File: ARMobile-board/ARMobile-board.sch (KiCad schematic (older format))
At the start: 10 parts

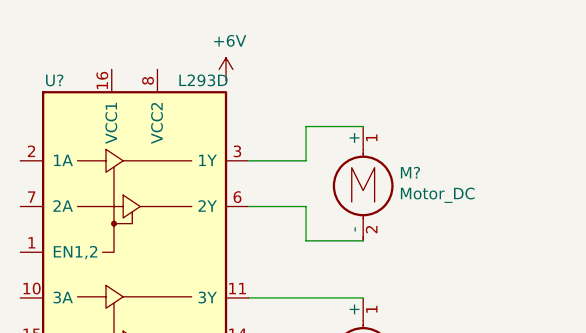
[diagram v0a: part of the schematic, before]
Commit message: Fixed schematic mistake (not connected pr)
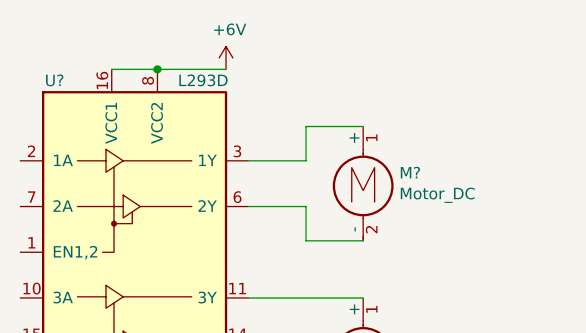
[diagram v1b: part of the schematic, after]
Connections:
- net +6V: now also U?.16 (VCC1), U?.8 (VCC2)
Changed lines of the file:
@@
 L power:+6V #PWR?
 U 1 1 60425D0B
-P 2650 800
-F 0 "#PWR?" H 2650 650 50  0001 C CNN
-F 1 "+6V" H 2665 973 50  0000 C CNN
-F 2 "" H 2650 800 50  0001 C CNN
-F 3 "" H 2650 800 50  0001 C CNN
-	1    2650 800
+P 2650 750
+F 0 "#PWR?" H 2650 600 50  0001 C CNN
+F 1 "+6V" H 2665 923 50  0000 C CNN
+F 2 "" H 2650 750 50  0001 C CNN
+F 3 "" H 2650 750 50  0001 C CNN
+	1    2650 750
 	1    0    0    -1
 $EndComp
@@
 	5000 1400 4500 1400
 Connection ~ 5000 1350
+Wire Wire Line
+	2650 750  2350 750
+Connection ~ 2350 750
+Wire Wire Line
+	2350 750  2150 750
 $EndSCHEMATC

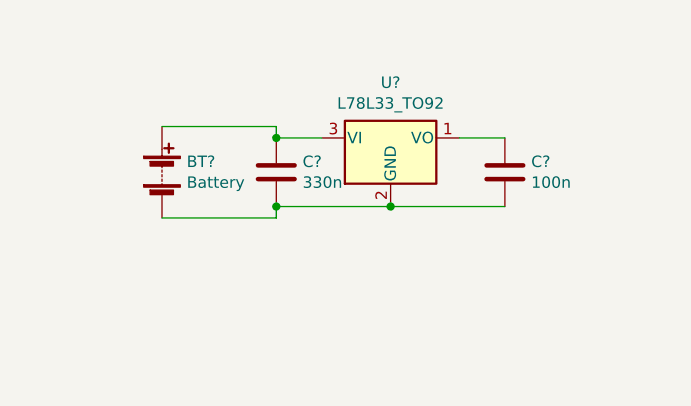
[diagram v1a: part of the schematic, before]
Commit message: Added power switch to schema
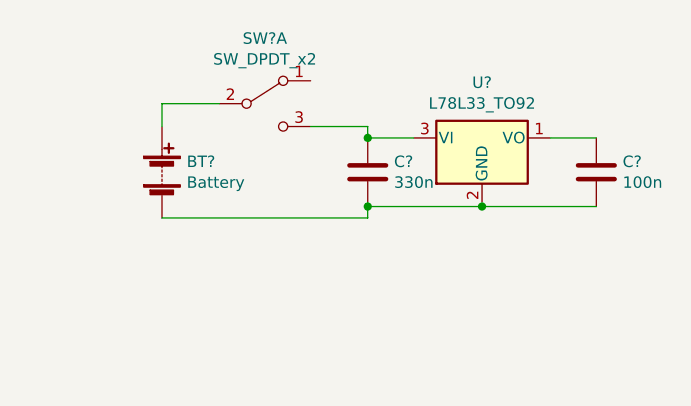
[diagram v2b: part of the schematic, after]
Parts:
- added SW?: SW_DPDT_x2, symbol Switch:SW_DPDT_x2
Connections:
- net at C?.1, U?.3 (VI): now also SW?.3 (C); no longer BT?.1 (+)
- new net: BT?.1 (+), SW?.2 (B)
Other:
- moved on the sheet: C?, U?
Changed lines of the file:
@@
 Wire Wire Line
 	3000 4100 2750 4100
+Wire Wire Line
+	2650 750  2350 750
+Connection ~ 2350 750
+Wire Wire Line
+	2350 750  2150 750
 $Comp
 L Device:Battery BT?
@@
 L Device:C C?
 U 1 1 60457EAB
-P 5000 1200
-F 0 "C?" H 5115 1246 50  0000 L CNN
-F 1 "330n" H 5115 1155 50  0000 L CNN
-F 2 "" H 5038 1050 50  0001 C CNN
-F 3 "~" H 5000 1200 50  0001 C CNN
-	1    5000 1200
+P 5400 1200
+F 0 "C?" H 5515 1246 50  0000 L CNN
+F 1 "330n" H 5515 1155 50  0000 L CNN
+F 2 "" H 5438 1050 50  0001 C CNN
+F 3 "~" H 5400 1200 50  0001 C CNN
+	1    5400 1200
 	1    0    0    -1
 $EndComp
@@
 L Device:C C?
 U 1 1 60458376
-P 6000 1200
-F 0 "C?" H 6115 1246 50  0000 L CNN
-F 1 "100n" H 6115 1155 50  0000 L CNN
-F 2 "" H 6038 1050 50  0001 C CNN
-F 3 "~" H 6000 1200 50  0001 C CNN
-	1    6000 1200
+P 6400 1200
+F 0 "C?" H 6515 1246 50  0000 L CNN
+F 1 "100n" H 6515 1155 50  0000 L CNN
+F 2 "" H 6438 1050 50  0001 C CNN
+F 3 "~" H 6400 1200 50  0001 C CNN
+	1    6400 1200
 	1    0    0    -1
 $EndComp
@@
 L Regulator_Linear:L78L33_TO92 U?
 U 1 1 60458CAC
-P 5500 1050
-F 0 "U?" H 5500 1292 50  0000 C CNN
-F 1 "L78L33_TO92" H 5500 1201 50  0000 C CNN
-F 2 "Package_TO_SOT_THT:TO-92_Inline" H 5500 1275 50  0001 C CIN
-F 3 "http://www.st.com/content/ccc/resource/technical/document/datasheet/15/55/e5/aa/23/5b/43/fd/CD00000446.pdf/files/CD00000446.pdf/jcr:content/translations/en.CD00000446.pdf" H 5500 1000 50  0001 C CNN
-	1    5500 1050
+P 5900 1050
+F 0 "U?" H 5900 1292 50  0000 C CNN
+F 1 "L78L33_TO92" H 5900 1201 50  0000 C CNN
+F 2 "Package_TO_SOT_THT:TO-92_Inline" H 5900 1275 50  0001 C CIN
+F 3 "http://www.st.com/content/ccc/resource/technical/document/datasheet/15/55/e5/aa/23/5b/43/fd/CD00000446.pdf/files/CD00000446.pdf/jcr:content/translations/en.CD00000446.pdf" H 5900 1000 50  0001 C CNN
+	1    5900 1050
 	1    0    0    -1
 $EndComp
 Wire Wire Line
-	5000 1050 5200 1050
+	5400 1050 5600 1050
 Wire Wire Line
-	5800 1050 6000 1050
+	6200 1050 6400 1050
 Wire Wire Line
-	6000 1350 5500 1350
-Connection ~ 5500 1350
+	6400 1350 5900 1350
+Connection ~ 5900 1350
 Wire Wire Line
-	5500 1350 5000 1350
+	5900 1350 5400 1350
 Wire Wire Line
-	4500 1000 5000 1000
+	5400 1000 5400 1050
+Connection ~ 5400 1050
 Wire Wire Line
-	5000 1000 5000 1050
-Connection ~ 5000 1050
+	5400 1350 5400 1400
+Connection ~ 5400 1350
 Wire Wire Line
-	5000 1350 5000 1400
+	4500 1400 5400 1400
+$Comp
+L Switch:SW_DPDT_x2 SW?
+U 1 1 6047A91C
+P 4950 900
+F 0 "SW?" H 4950 1185 50  0000 C CNN
+F 1 "SW_DPDT_x2" H 4950 1094 50  0000 C CNN
+F 2 "" H 4950 900 50  0001 C CNN
+F 3 "~" H 4950 900 50  0001 C CNN
+	1    4950 900
+	1    0    0    -1
+$EndComp
 Wire Wire Line
-	5000 1400 4500 1400
-Connection ~ 5000 1350
+	4750 900  4500 900
 Wire Wire Line
-	2650 750  2350 750
-Connection ~ 2350 750
+	4500 900  4500 1000
 Wire Wire Line
-	2350 750  2150 750
+	5150 1000 5400 1000
 $EndSCHEMATC
